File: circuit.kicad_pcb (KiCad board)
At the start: 4 copper layers, 175 x 119.5 mm, 207 parts, among them J201 Barrel_Jack, J301 FX_R_1, J302 FX_R_2, J303 FX_R_3, J304 FX_R_4, J305 FX_R_5, J306 FX_R_6, J307 FX_R_7, J308 FX_R_8, J309 FX_S_1, J310 FX_S_2, J311 FX_S_3, J312 FX_S_4, J313 FX_S_5, J314 FX_S_6, J315 FX_S_7, J316 FX_S_8, J317 Guitar_In, J318 Amp_Out, SW101 Pedal_1, SW102 Pedal_6, SW103 Pedal_2, SW104 Pedal_7, SW105 Pedal_3, SW106 Pedal_8, SW107 Pedal_4, SW108 Program, SW109 Pedal_5, SW110 Preset, U101 ESP32-S3-DevKitC, U201 TMA-1215D, U202 LM7805_TO220, U203 LM7905_TO220, U204 LM1117T-3.3, U301 TL072, U302 TL072, U303 TL072, U304 TL072, U305 TL072, U306 TL072, U307 TL072, U308 TL072, U309 TL072, U401 ADG419BN, U402 CD4051B, U501 CD4051B, U502 CD4051B, U503 CD4051B, U504 CD4051B, U601 CD4051B, U602 CD4051B, U603 CD4051B, U604 CD4051B, U701 74HC595, U702 74HC595, U703 74HC595, U704 74HC595, U801 74HC595, U802 74HC595, U901 74HC595, U902 74HC595

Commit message: New cooler (thermally) power supply.
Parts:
- removed C203, C207: 10uF, Capacitor_THT:CP_Radial_D5.0mm_P2.50mm
- removed U204: LM1117T-3.3, Package_TO_SOT_THT:TO-220-3_Vertical
- added C211: 100uF 50v, Capacitor_THT:CP_Radial_D5.0mm_P2.50mm, F.Cu at (38.5, 71.7)
- added D202: 1N5822, Diode_THT:D_DO-41_SOD81_P10.16mm_Horizontal, F.Cu at (169.4, 155.0)
- added D203: 1N5819, Diode_THT:D_DO-41_SOD81_P10.16mm_Horizontal, F.Cu at (39.0, 130.4)
- added L201: 150uH, Inductor_THT:L_Radial_D10.0mm_P5.00mm_Fastron_07M, F.Cu at (173.5, 143.5)
- added L202: 220uH, Inductor_THT:L_Radial_D10.0mm_P5.00mm_Fastron_07M, F.Cu at (39.0, 122.0)
- added R201: 1.5, Resistor_THT:R_Axial_DIN0207_L6.3mm_D2.5mm_P7.62mm_Horizontal, F.Cu at (37.5, 102.5)
- added R202: 1k, Resistor_THT:R_Axial_DIN0207_L6.3mm_D2.5mm_P7.62mm_Horizontal, F.Cu at (37.5, 107.2)
- added R203: 11k, Resistor_THT:R_Axial_DIN0207_L6.3mm_D2.5mm_P7.62mm_Horizontal, F.Cu at (37.5, 112.0)
- added U205: LM2576HVT-5, Package_TO_SOT_THT:TO-220-5_Vertical, F.Cu at (189.9, 154.0)
- C201: value 0.33uF -> 0.1uF
- C202: value 0.33uF -> 1uF
- C204: value 0.1uF -> 100uF 50v; footprint Capacitor_THT:C_Disc_D5.0mm_W2.5mm_P2.50mm -> Capacitor_THT:CP_Radial_D5.0mm_P2.50mm
- C205: value 0.1uF -> 1uF
- C208: value 10uF -> 220uF 16v
- C209: value 100uF -> 100uF 50v
- C210: value 0.1uF -> 470pF
- U201: value TMA-1215D -> MC34063AP; footprint Converter_DCDC:Converter_DCDC_TRACO_TMA-05xxD_12xxD_Dual_THT -> Package_DIP:DIP-8_W7.62mm
- U202: value LM7805_TO220 -> LM7815_TO220
- moved C210 113.6 mm to (41.5, 85.2)
- moved C204 110.3 mm to (38.5, 78.0), turned to 90 degrees
- moved U201 99.4 mm to (37.4, 90.0), turned to 0 degrees
- moved JP101 64.9 mm to (199.5, 91.5), turned to 0 degrees
- moved R101 35.4 mm to (196.8, 105.5)
- moved Disp101 31.8 mm to (194.0, 91.0)
- moved RV101 30.5 mm to (195.5, 113.5)
- moved D201 23.6 mm to (188.4, 138.0), turned to 0 degrees
- moved F201 20.9 mm to (195.0, 145.0), turned to -90 degrees
- moved C202 12.0 mm to (204.8, 136.0), turned to 90 degrees
- moved C201 8.14 mm to (161.0, 142.5)
- moved C206 5.55 mm to (204.8, 130.0)
- moved C209 2.50 mm to (179.0, 147.5)
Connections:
- C201 pad 1: /Power/12V_to_5V -> +15V
- C201 pad 2: VIN_12V -> AGND
- C202 pad 1: /Power/12V_to_-5V -> GND
- C202 pad 2: VIN_12V -> -15V
- C204 pad 1: AGND -> VIN_24V
- C204 pad 2: -15V -> AGND
- C205 pad 1: +5V -> VIN_24V
- C205 pad 2: Net-(U202-VO) -> AGND
- C206 pad 1: -5V -> GND
- C206 pad 2: Net-(U203-VO) -> -5V
- C208 pad 1: VIN_12V -> +5V
- C209 pad 1: VIN_12V -> VIN_24V
- C210 pad 1: +15V -> Net-(U201-TC)
- D201 pad 1: /Power/12V_RAW_2 -> VIN_24V
- D201 pad 2: /Power/12V_RAW_1 -> /Power/24V_RAW_2
- F201 pad 1: VIN_12V -> /Power/24V_RAW_2
- F201 pad 2: /Power/12V_RAW_2 -> /Power/24V_RAW_1
- J201 pad 1: /Power/12V_RAW_1 -> /Power/24V_RAW_1
- U101 pad 1: unconnected-(U101-3V3-Pad1)_1 -> 3.3V
- U101 pad 2: unconnected-(U101-3V3-Pad1) -> 3.3V
- U201 pad 1: VIN_12V -> -15V
- U201 pad 4: -15V -> AGND
- U201 pad 5: unconnected-(U201-Com-Pad5) -> Net-(U201-Vfb)
- U201 pad 6: +15V -> VIN_24V
- U202 pad 1: /Power/12V_to_5V -> VIN_24V
- U202 pad 2: GND -> AGND
- U202 pad 3: Net-(U202-VO) -> +15V
- U203 pad 2: /Power/12V_to_-5V -> -15V
- U203 pad 3: Net-(U203-VO) -> -5V
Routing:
- net VIN_24V: track 0.00 -> 227.0 mm
- net -15V: track 107.0 -> 296.8 mm
- net VIN_12V: track 157.8 -> 0.00 mm
- net +15V: track 116.5 -> 267.1 mm
- net AGND: track 671.4 -> 779.4 mm
- net +5V: track 117.8 -> 225.3 mm
- net Net-(Disp101-SDA): track 131.8 -> 43.2 mm
- net /IO Routing/U901_Q0: track 146.8 -> 233.8 mm
- net Net-(Disp101-SCL): track 128.5 -> 43.2 mm
- net Net-(U101-GPIO6/ADC1_CH5): track 138.9 -> 87.6 mm
- net /IO Routing/U701_Q0: track 98.1 -> 148.7 mm
- net Net-(Disp101-VCC): track 51.2 -> 6.78 mm
- net Net-(U101-GPIO13/ADC2_CH2): track 88.0 -> 129.6 mm
- net /Matrix Shift Registers/U703_Q7: track 85.3 -> 126.9 mm
- net Net-(U101-GPIO12/ADC2_CH1): track 81.2 -> 120.0 mm
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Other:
- board size 175 x 119.5 mm -> 181 x 119.5 mm

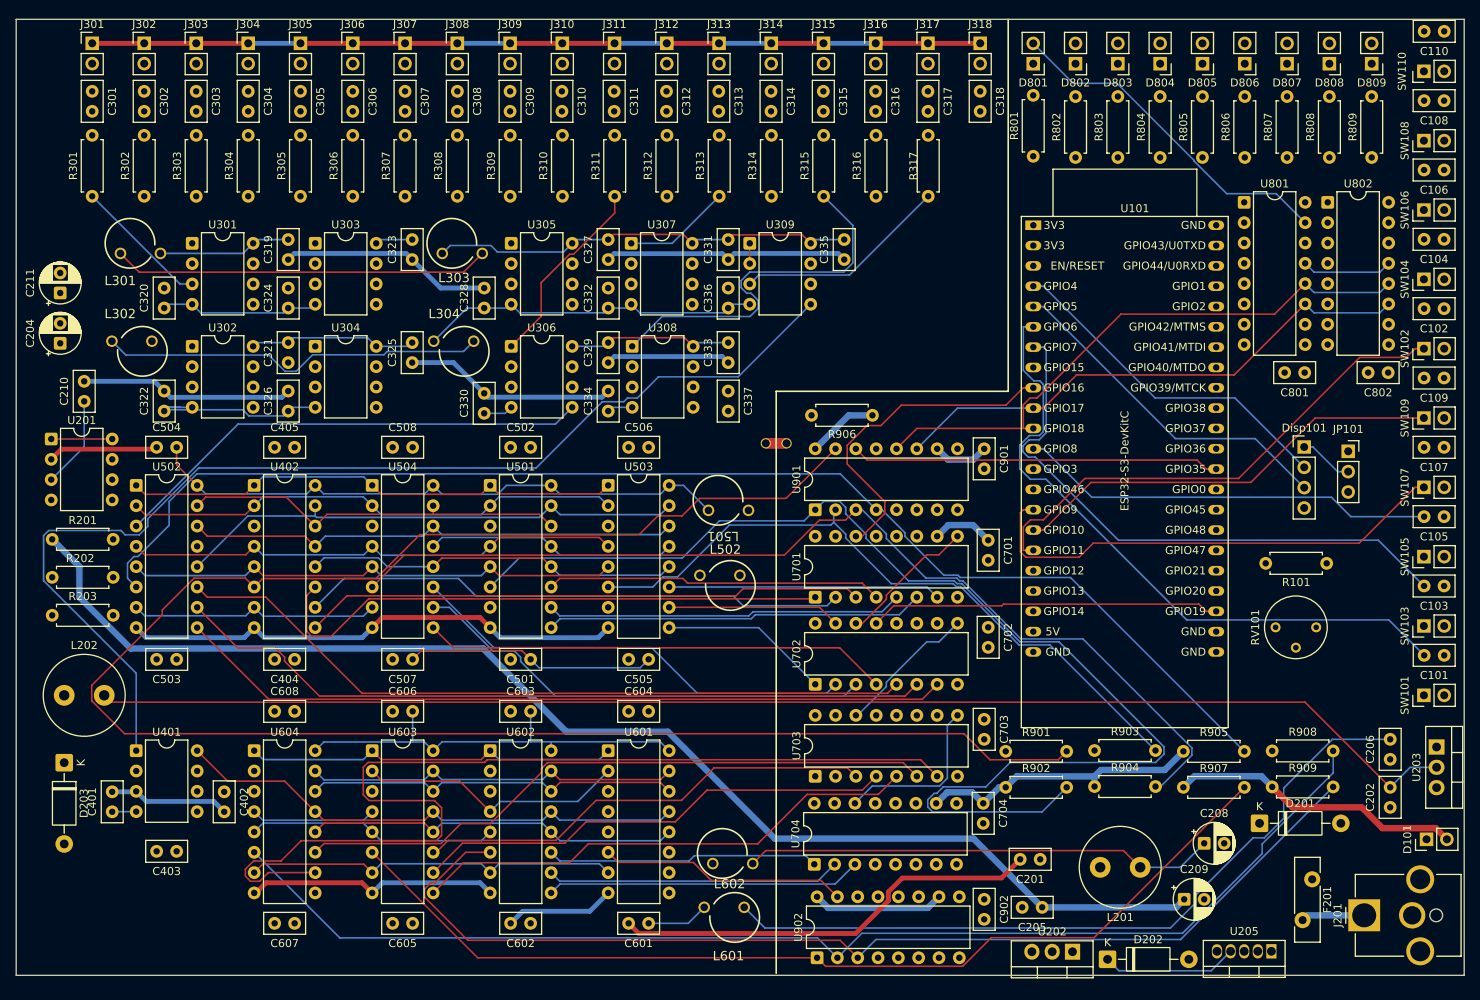
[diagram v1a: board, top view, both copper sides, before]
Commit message: Removed un-needed inhibit from amp out. thereby simplifying the shift registers.
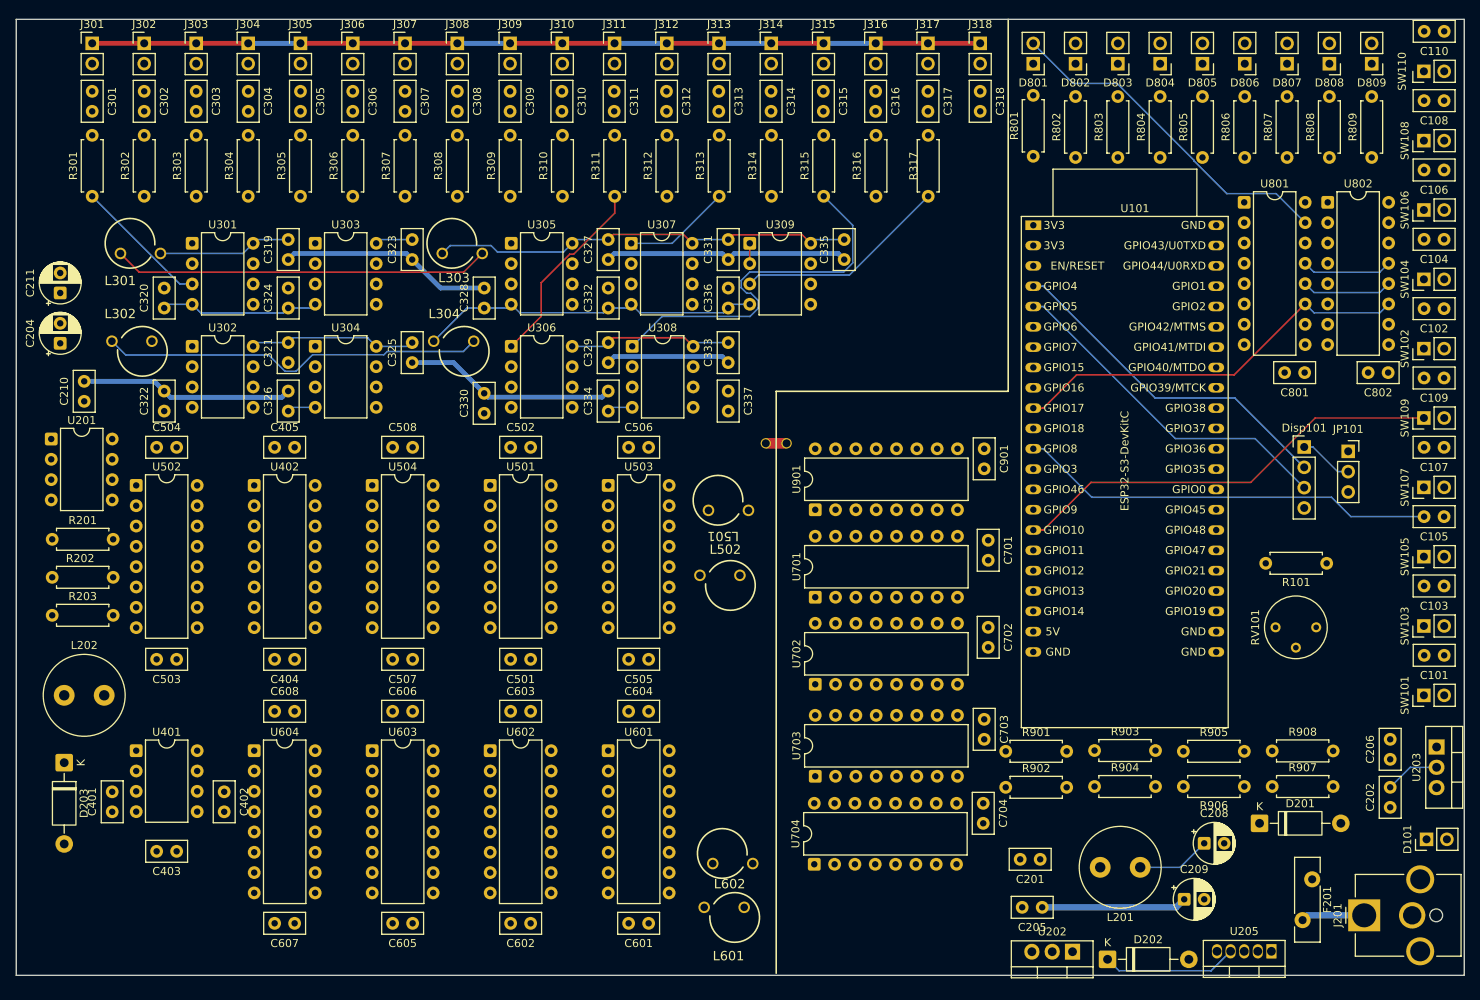
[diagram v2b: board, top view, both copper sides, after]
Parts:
- removed C902: 0.1uF, Capacitor_THT:C_Disc_D5.0mm_W2.5mm_P2.50mm
- removed R909: 10k, Resistor_THT:R_Axial_DIN0207_L6.3mm_D2.5mm_P7.62mm_Horizontal
- removed U902: 74HC595, Package_DIP:DIP-16_W7.62mm
- moved R906 65.7 mm to (186.5, 133.4)
- moved R907 11.1 mm to (190.0, 133.4)
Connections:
- R901 pad 2: /IO Routing/U901_Q0 -> /Inhibit Registers/U901_Q0
- R902 pad 2: /IO Routing/U901_Q1 -> /Inhibit Registers/U901_Q1
- R903 pad 2: /IO Routing/U901_Q2 -> /Inhibit Registers/U901_Q2
- R904 pad 2: /IO Routing/U901_Q3 -> /Inhibit Registers/U901_Q3
- R905 pad 2: /IO Routing/U901_Q4 -> /Inhibit Registers/U901_Q4
- R906 pad 2: /Inhibit Registers/U902_Q0 -> /Inhibit Registers/U901_Q5
- R907 pad 2: /Inhibit Registers/U902_Q1 -> /Inhibit Registers/U901_Q6
- R908 pad 2: /Inhibit Registers/U902_Q2 -> /Inhibit Registers/U901_Q7
- U402 pad 6: /IO Routing/U901_Q0 -> AGND
- U501 pad 6: /IO Routing/U901_Q1 -> /Inhibit Registers/U901_Q0
- U502 pad 6: /IO Routing/U901_Q4 -> /Inhibit Registers/U901_Q3
- U503 pad 6: /IO Routing/U901_Q2 -> /Inhibit Registers/U901_Q1
- U504 pad 6: /IO Routing/U901_Q3 -> /Inhibit Registers/U901_Q2
- U601 pad 6: /Inhibit Registers/U902_Q0 -> /Inhibit Registers/U901_Q4
- U602 pad 6: /Inhibit Registers/U902_Q3 -> /Inhibit Registers/U901_Q7
- U603 pad 6: /Inhibit Registers/U902_Q1 -> /Inhibit Registers/U901_Q5
- U604 pad 6: /Inhibit Registers/U902_Q2 -> /Inhibit Registers/U901_Q6
- U901 pad 1: /IO Routing/U901_Q1 -> /Inhibit Registers/U901_Q1
- U901 pad 15: /IO Routing/U901_Q0 -> /Inhibit Registers/U901_Q0
- U901 pad 2: /IO Routing/U901_Q2 -> /Inhibit Registers/U901_Q2
- U901 pad 3: /IO Routing/U901_Q3 -> /Inhibit Registers/U901_Q3
- U901 pad 4: /IO Routing/U901_Q4 -> /Inhibit Registers/U901_Q4
- U901 pad 5: unconnected-(U901-QF-Pad5) -> /Inhibit Registers/U901_Q5
- U901 pad 6: unconnected-(U901-QG-Pad6) -> /Inhibit Registers/U901_Q6
- U901 pad 7: unconnected-(U901-QH-Pad7) -> /Inhibit Registers/U901_Q7
- U901 pad 9: Net-(U901-QH') -> unconnected-(U901-QH&apos;-Pad9)
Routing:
- net AGND: track 779.4 -> 345.7 mm
- net 3.3V: track 415.1 -> 52.8 mm
- net /IO Routing/U901_Q0: track 233.8 -> 0.00 mm
- net -15V: track 296.8 -> 66.4 mm
- net +15V: track 267.1 -> 47.2 mm
- net FX_R_6: track 191.3 -> 2.54 mm
- net FX_R_3: track 185.0 -> 2.54 mm
- net FX_R_1: track 182.1 -> 0.00 mm
- net GUITAR_IN: track 177.7 -> 0.00 mm
- net FX_R_5: track 176.1 -> 0.00 mm
- net VIN_24V: track 227.0 -> 51.4 mm
- net FX_R_8: track 171.4 -> 2.54 mm
- net /IO Routing/U901_Q4: track 164.0 -> 0.00 mm
- net +5V_F: track 162.1 -> 0.00 mm
- net FX_R_2: track 161.3 -> 2.54 mm
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
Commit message: Removed LED Shift registers and replaced them with PCA9685 PWM controllers, Also changed LEDs to RGB LEDs.
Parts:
- removed C801, C802: 0.1uF, Capacitor_THT:C_Disc_D5.0mm_W2.5mm_P2.50mm
- removed D801: Pedal_1, Connector_PinHeader_2.54mm:PinHeader_1x02_P2.54mm_Vertical
- removed D802: Pedal_2, Connector_PinHeader_2.54mm:PinHeader_1x02_P2.54mm_Vertical
- removed D803: Pedal_3, Connector_PinHeader_2.54mm:PinHeader_1x02_P2.54mm_Vertical
- removed D804: Pedal_4, Connector_PinHeader_2.54mm:PinHeader_1x02_P2.54mm_Vertical
- removed D805: Status, Connector_PinHeader_2.54mm:PinHeader_1x02_P2.54mm_Vertical
- removed D806: Pedal_5, Connector_PinHeader_2.54mm:PinHeader_1x02_P2.54mm_Vertical
- removed D807: Pedal_6, Connector_PinHeader_2.54mm:PinHeader_1x02_P2.54mm_Vertical
- removed D808: Pedal_7, Connector_PinHeader_2.54mm:PinHeader_1x02_P2.54mm_Vertical
- removed D809: Pedal_8, Connector_PinHeader_2.54mm:PinHeader_1x02_P2.54mm_Vertical
- removed R801, R802, R803, R804, R805, R806, R807, R808, R809: 150, Resistor_THT:R_Axial_DIN0207_L6.3mm_D2.5mm_P7.62mm_Horizontal
- removed U801, U802: 74HC595, Package_DIP:DIP-16_W7.62mm
- added J801: Conn_01x06_Pin, Connector_PinHeader_2.54mm:PinHeader_1x06_P2.54mm_Vertical, F.Cu at (172.2, 112.0)
- moved JP101 37.7 mm to (178.0, 122.5), turned to -90 degrees
- moved R101 33.4 mm to (167.8, 122.0)
- moved C209 31.5 mm to (147.5, 149.0)
- moved Disp101 29.7 mm to (179.8, 117.0), turned to -90 degrees
- moved RV101 29.0 mm to (166.5, 114.5)
- moved C201 27.4 mm to (134.0, 147.0), turned to 0 degrees
- moved F201 24.1 mm to (170.9, 142.9), turned to 0 degrees
- moved U202 24.0 mm to (141.1, 153.5)
- moved C208 21.4 mm to (164.5, 153.5)
- moved C205 18.3 mm to (143.0, 147.0)
- moved C101 17.0 mm to (194.5, 118.0)
- moved C102 17.0 mm to (194.5, 74.7)
- moved C103 17.0 mm to (194.5, 109.3)
- moved C104 17.0 mm to (194.5, 66.0)
- moved C105 17.0 mm to (194.5, 100.7)
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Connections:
- net Net-(Disp101-SCL) renamed SCL
- net Net-(Disp101-SDA) renamed SDA
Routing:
- net AGND: track 345.7 -> 791.3 mm
- net 3.3V: track 52.8 -> 280.1 mm
- net -15V: track 66.4 -> 287.5 mm
- net FX_R_6: track 2.54 -> 195.1 mm
- net FX_R_3: track 2.54 -> 187.9 mm
- net /Inhibit Registers/U901_Q6: track 0.00 -> 185.2 mm
- net FX_R_1: track 0.00 -> 183.6 mm
- net /Inhibit Registers/U901_Q2: track 0.00 -> 179.6 mm
- net FX_R_5: track 0.00 -> 176.0 mm
- net GUITAR_IN: track 0.00 -> 173.3 mm
- net FX_R_7: track 2.54 -> 172.1 mm
- net FX_R_8: track 2.54 -> 169.4 mm
- net VIN_24V: track 51.4 -> 212.3 mm
- net FX_R_2: track 2.54 -> 160.2 mm
- net FX_R_4: track 0.00 -> 151.5 mm
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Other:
- board size 181 x 119.5 mm -> 165 x 119.5 mm
